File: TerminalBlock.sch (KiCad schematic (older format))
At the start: 0 parts

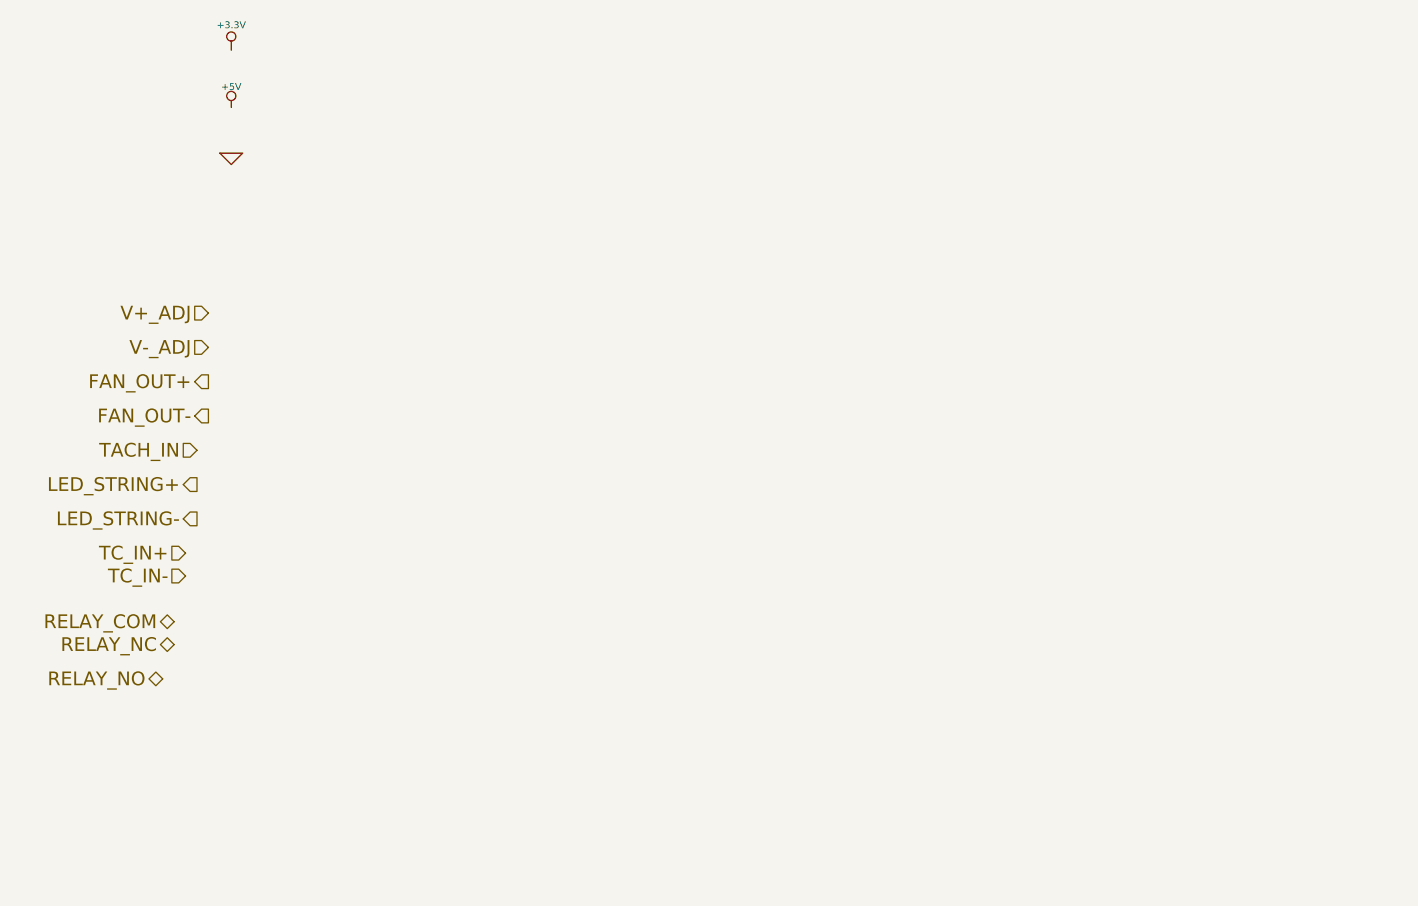
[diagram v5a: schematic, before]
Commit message: Completed terminal block placement and footprints
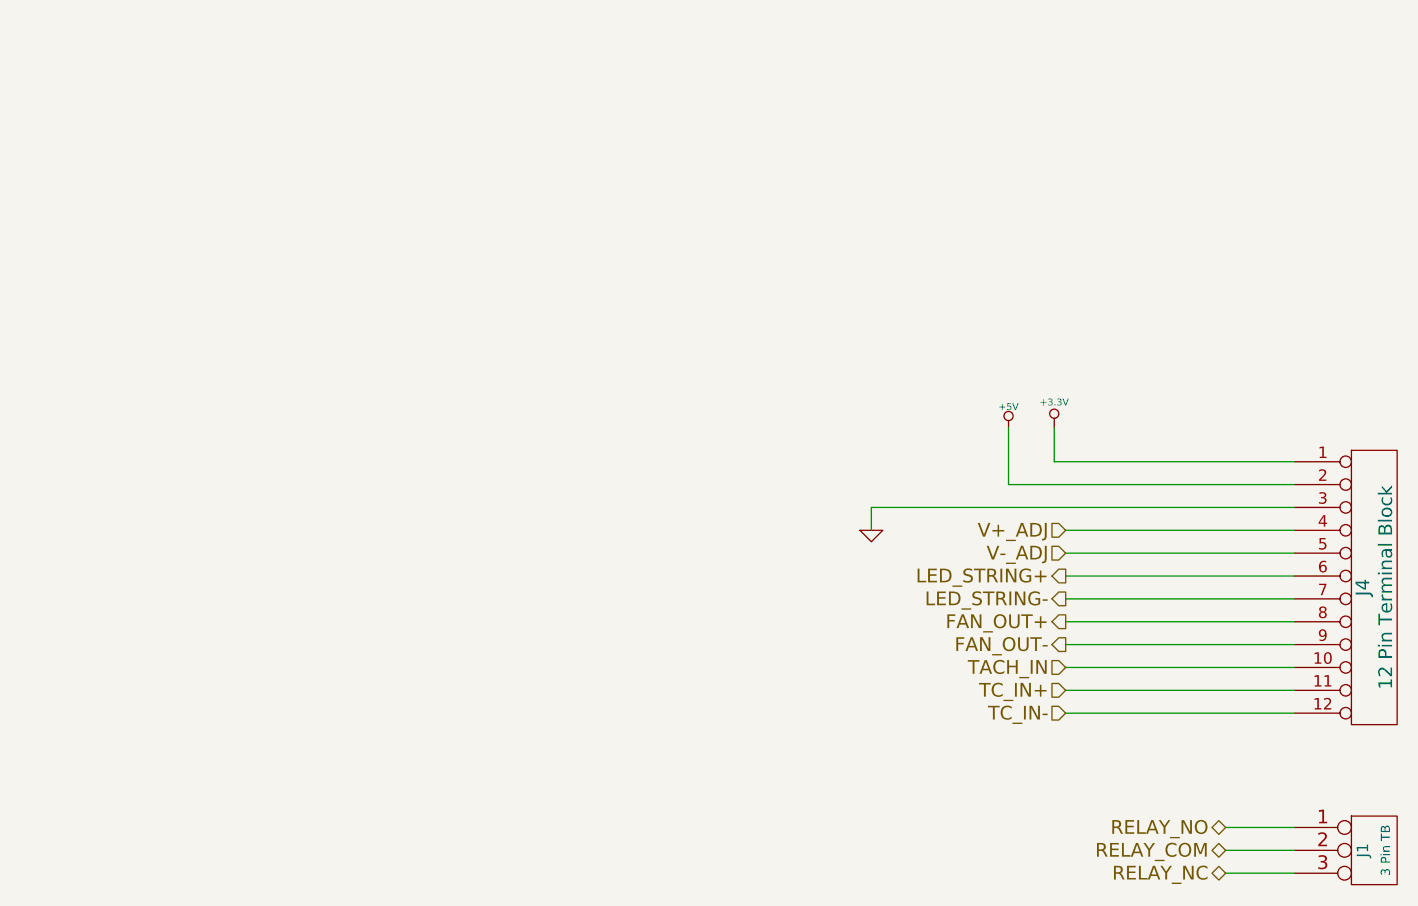
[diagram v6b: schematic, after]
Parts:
- added J1: 3 Pin TB, symbol CONN_3
- added J4: 12 Pin Terminal Block, symbol CONN_12
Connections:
- net +3.3V: now also J4.1 (P1)
- net +5V: now also J4.2 (P2)
- net FAN_OUT+: now also J4.8 (P8)
- net FAN_OUT-: now also J4.9 (P9)
- net GND: now also J4.3 (P3)
- net LED_STRING+: now also J4.6 (P6)
- net LED_STRING-: now also J4.7 (P7)
- net RELAY_COM: now also J1.2 (PM)
- net RELAY_NC: now also J1.3 (P3)
- net RELAY_NO: now also J1.1 (P1)
- net TACH_IN: now also J4.10 (P10)
- net TC_IN+: now also J4.11 (P11)
- net TC_IN-: now also J4.12 (P12)
- net V+_ADJ: now also J4.4 (P4)
- net V-_ADJ: now also J4.5 (P5)
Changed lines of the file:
@@
 $Descr A4 11693 8268
 encoding utf-8
-Sheet 6 9
+Sheet 8 9
 Title ""
-Date "23 feb 2014"
+Date "2 mar 2014"
 Rev ""
 Comp ""
@@
 Comment4 ""
 $EndDescr
-Text HLabel 1750 2300 0    60   Input ~ 0
+Text HLabel 5500 3250 0    60   Input ~ 0
 V+_ADJ
-Text HLabel 1750 2450 0    60   Input ~ 0
+Text HLabel 5500 3350 0    60   Input ~ 0
 V-_ADJ
-Text HLabel 1750 2600 0    60   Output ~ 0
+Text HLabel 5500 3650 0    60   Output ~ 0
 FAN_OUT+
-Text HLabel 1750 2750 0    60   Output ~ 0
+Text HLabel 5500 3750 0    60   Output ~ 0
 FAN_OUT-
-Text HLabel 1700 2900 0    60   Input ~ 0
+Text HLabel 5500 3850 0    60   Input ~ 0
 TACH_IN
-Text HLabel 1700 3050 0    60   Output ~ 0
+Text HLabel 5500 3450 0    60   Output ~ 0
 LED_STRING+
-Text HLabel 1700 3200 0    60   Output ~ 0
+Text HLabel 5500 3550 0    60   Output ~ 0
 LED_STRING-
-Text HLabel 1650 3350 0    60   Input ~ 0
+Text HLabel 5500 3950 0    60   Input ~ 0
 TC_IN+
-Text HLabel 1650 3450 0    60   Input ~ 0
+Text HLabel 5500 4050 0    60   Input ~ 0
 TC_IN-
-Text HLabel 1600 3650 0    60   BiDi ~ 0
+Text HLabel 6200 4650 0    60   BiDi ~ 0
 RELAY_COM
-Text HLabel 1600 3750 0    60   BiDi ~ 0
+Text HLabel 6200 4750 0    60   BiDi ~ 0
 RELAY_NC
-Text HLabel 1550 3900 0    60   BiDi ~ 0
+Text HLabel 6200 4550 0    60   BiDi ~ 0
 RELAY_NO
 $Comp
-L +3.3V #PWR59
+L +3.3V #PWR057
 U 1 1 52F9CCB5
-P 1850 1150
-F 0 "#PWR59" H 1850 1110 30  0001 C CNN
-F 1 "+3.3V" H 1850 1260 30  0000 C CNN
-F 2 "" H 1850 1150 60  0000 C CNN
-F 3 "" H 1850 1150 60  0000 C CNN
-	1    1850 1150
+P 5450 2800
+F 0 "#PWR057" H 5450 2760 30  0001 C CNN
+F 1 "+3.3V" H 5450 2910 30  0000 C CNN
+F 2 "" H 5450 2800 60  0000 C CNN
+F 3 "" H 5450 2800 60  0000 C CNN
+	1    5450 2800
 	1    0    0    -1
 $EndComp
 $Comp
-L +5V #PWR60
+L +5V #PWR058
 U 1 1 52F9CCC4
-P 1850 1400
-F 0 "#PWR60" H 1850 1490 20  0001 C CNN
-F 1 "+5V" H 1850 1490 30  0000 C CNN
-F 2 "" H 1850 1400 60  0000 C CNN
-F 3 "" H 1850 1400 60  0000 C CNN
-	1    1850 1400
+P 5250 2800
+F 0 "#PWR058" H 5250 2890 20  0001 C CNN
+F 1 "+5V" H 5250 2890 30  0000 C CNN
+F 2 "" H 5250 2800 60  0000 C CNN
+F 3 "" H 5250 2800 60  0000 C CNN
+	1    5250 2800
 	1    0    0    -1
 $EndComp
 $Comp
-L GND #PWR61
+L GND #PWR059
 U 1 1 52F9CCD3
-P 1850 1600
-F 0 "#PWR61" H 1850 1600 30  0001 C CNN
-F 1 "GND" H 1850 1530 30  0001 C CNN
-F 2 "" H 1850 1600 60  0000 C CNN
-F 3 "" H 1850 1600 60  0000 C CNN
-	1    1850 1600
+P 4650 3250
+F 0 "#PWR059" H 4650 3250 30  0001 C CNN
+F 1 "GND" H 4650 3180 30  0001 C CNN
+F 2 "" H 4650 3250 60  0000 C CNN
+F 3 "" H 4650 3250 60  0000 C CNN
+	1    4650 3250
 	1    0    0    -1
 $EndComp
+$Comp
+L CONN_12 J4
+U 1 1 531356A5
+P 6850 3500
+F 0 "J4" V 6800 3500 60  0000 C CNN
+F 1 "12 Pin Terminal Block" V 6900 3500 60  0000 C CNN
+F 2 "" H 6850 3500 60  0000 C CNN
+F 3 "" H 6850 3500 60  0000 C CNN
+F 4 "OSTTE120104" H 6850 3500 60  0001 C CNN "Part Number"
+F 5 "On Shore Technology Inc" H 6850 3500 60  0001 C CNN "MFG Name"
+	1    6850 3500
+	1    0    0    -1
+$EndComp
+Wire Wire Line
+	6500 2950 5450 2950
+Wire Wire Line
+	5450 2950 5450 2800
+Wire Wire Line
+	6500 3050 5250 3050
+Wire Wire Line
+	5250 3050 5250 2800
+Wire Wire Line
+	4650 3250 4650 3150
+Wire Wire Line
+	4650 3150 6500 3150
+Wire Wire Line
+	5500 3250 6500 3250
+Wire Wire Line
+	5500 3350 6500 3350
+Wire Wire Line
+	5500 3450 6500 3450
+Wire Wire Line
+	5500 3550 6500 3550
+Wire Wire Line
+	5500 3650 6500 3650
+Wire Wire Line
+	5500 3750 6500 3750
+Wire Wire Line
+	5500 3850 6500 3850
+Wire Wire Line
+	5500 3950 6500 3950
+Wire Wire Line
+	5500 4050 6500 4050
+$Comp
+L CONN_3 J1
+U 1 1 53135784
+P 6850 4650
+F 0 "J1" V 6800 4650 50  0000 C CNN
+F 1 "3 Pin TB" V 6900 4650 40  0000 C CNN
+F 2 "" H 6850 4650 60  0000 C CNN
+F 3 "" H 6850 4650 60  0000 C CNN
+F 4 "1935174" H 6850 4650 60  0001 C CNN "Part Number"
+F 5 "Phoenix Contact" H 6850 4650 60  0001 C CNN "MFG Name"
+	1    6850 4650
+	1    0    0    -1
+$EndComp
+Wire Wire Line
+	6200 4550 6500 4550
+Wire Wire Line
+	6200 4650 6500 4650
+Wire Wire Line
+	6200 4750 6500 4750
 $EndSCHEMATC
